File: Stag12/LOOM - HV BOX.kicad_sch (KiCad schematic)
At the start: 15 parts

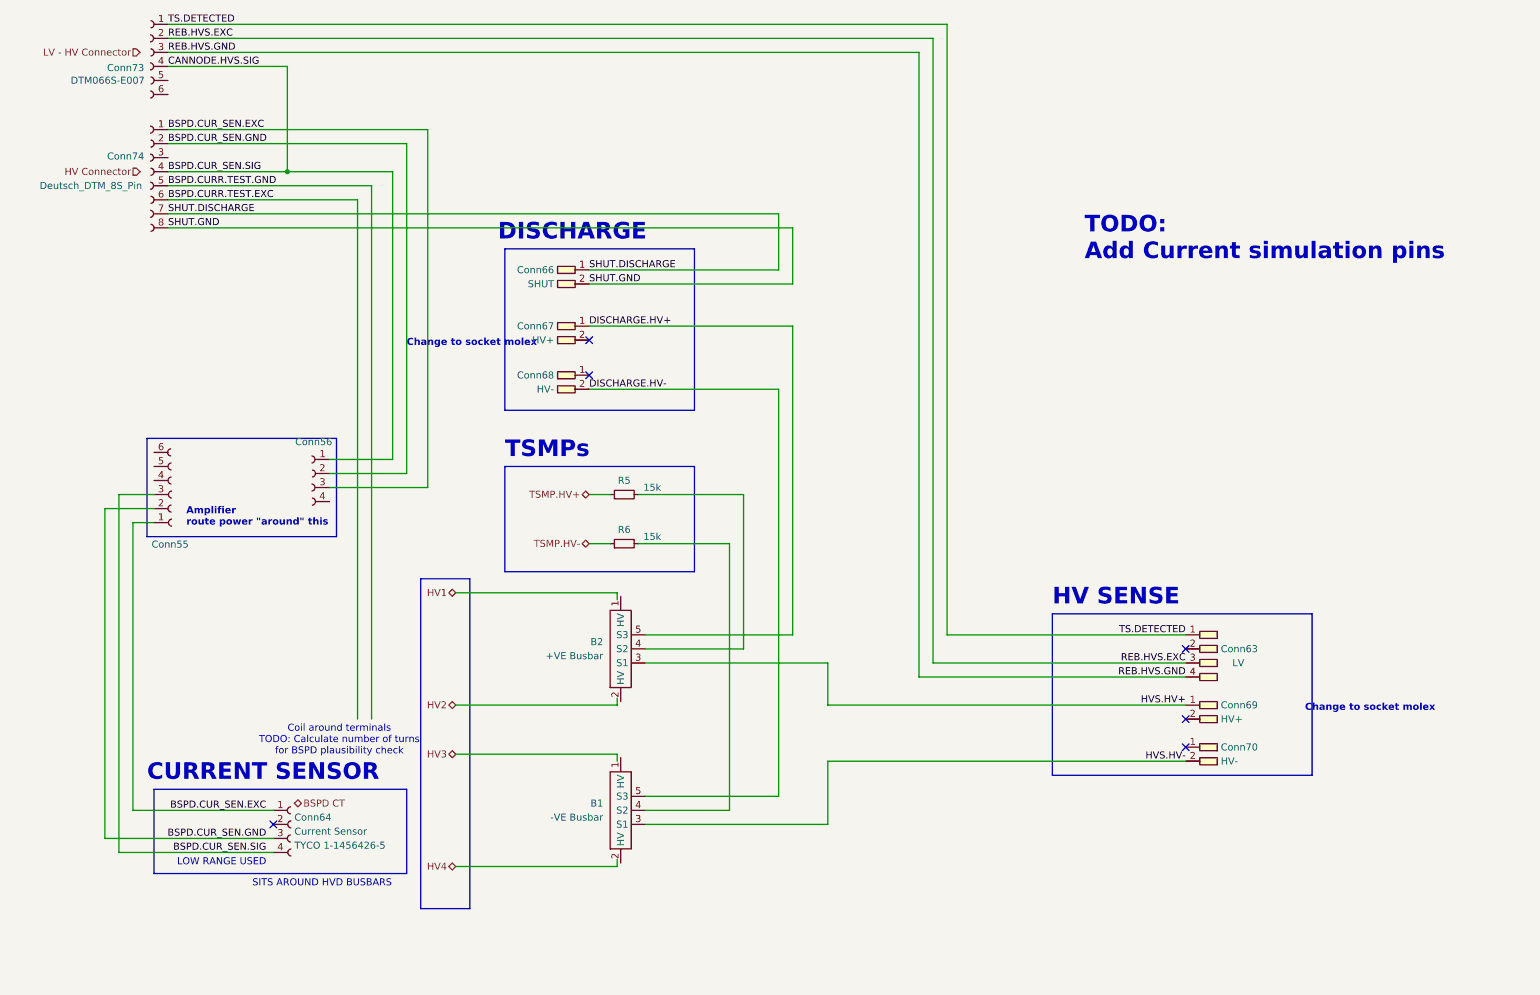
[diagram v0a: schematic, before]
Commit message: HV Box Loom Complete
Moved HVD into HV box, added grounds for cable shield
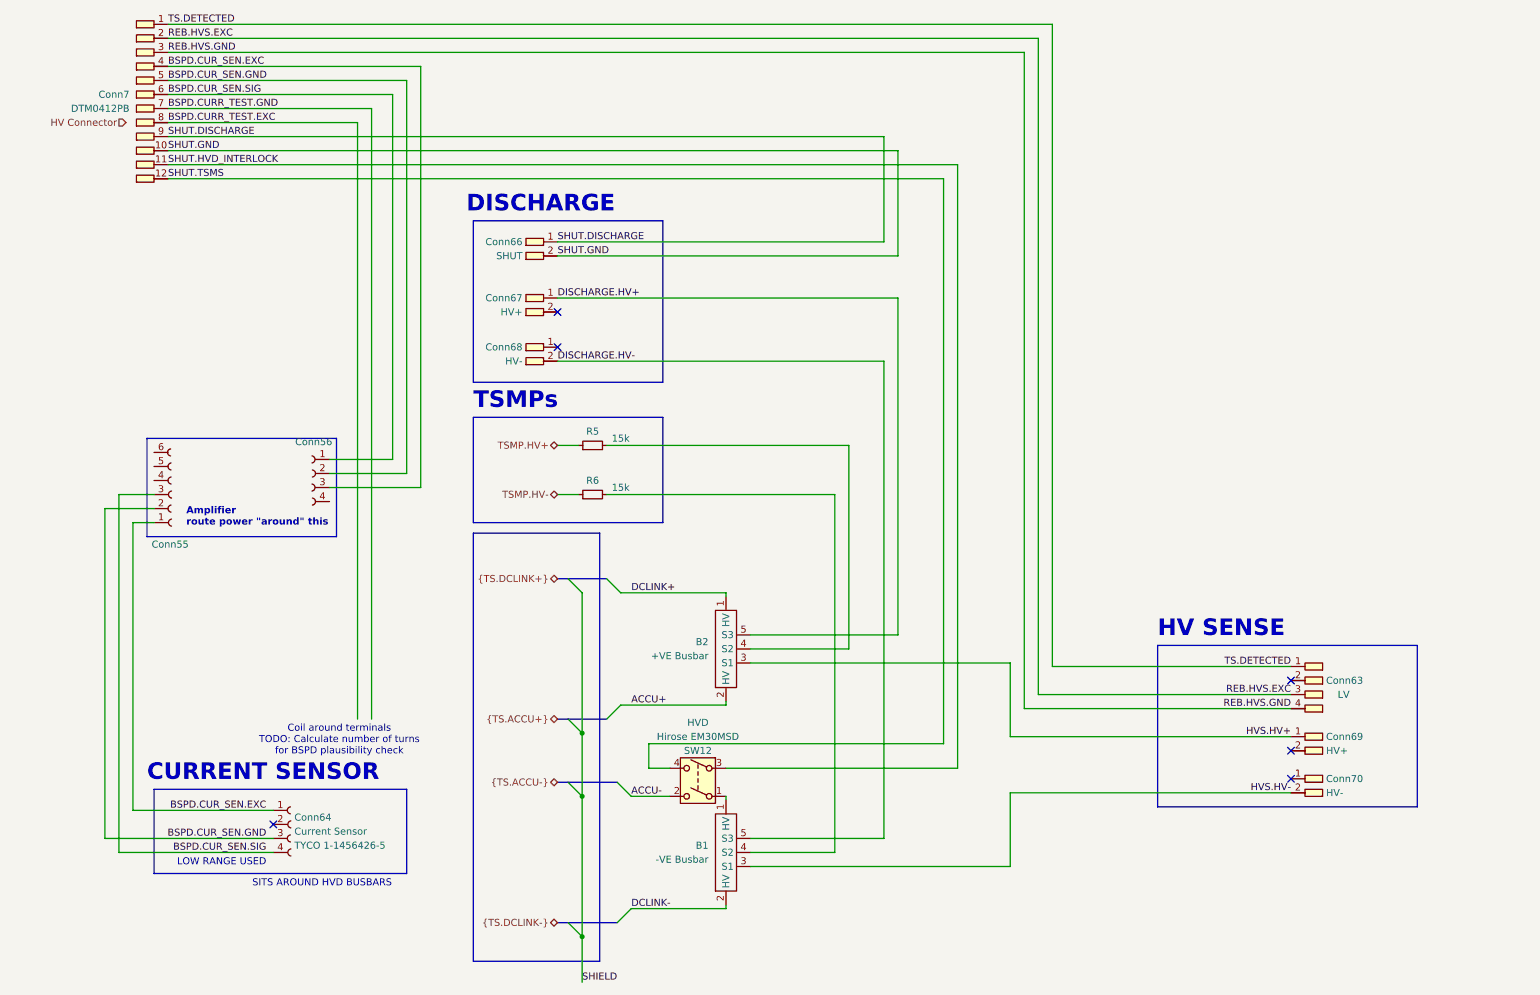
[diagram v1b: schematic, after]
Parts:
- removed Conn73: Deutsch_DTM_12S_Pin, symbol Connectors_SUFST:Deutsch_DTM_6S_Pin
- removed Conn74: Deutsch_DTM_8S_Pin, symbol Connectors_SUFST:Molex_8x1S_Recepticle
- added Conn7: Deutsch_DTM_12P_Pin, symbol Connectors_SUFST:Deutsch_DTM_12P_Pin
- added SW12: Hirose EM30MSD, symbol Switch:SW_DPST
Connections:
- net BSPD.CUR_SEN.EXC: now also Conn7.4
- net BSPD.CUR_SEN.GND: now also Conn7.5
- net BSPD.CUR_SEN.SIG: now also Conn7.6
- net REB.HVS.EXC: now also Conn7.2
- net REB.HVS.GND: now also Conn7.3
- net SHUT.DISCHARGE: now also Conn7.9
- net SHUT.GND: now also Conn7.10
- net TS.DETECTED: now also Conn7.1
- net at B1.1 (HV): now also SW12.1
- net DCLINK-: now reaches B1.2 (HV)
- net DCLINK+: now reaches B2.1 (HV)
- net ACCU+: now reaches B2.2 (HV)
- new net ACCU-: SW12.2
- new net BSPD.CURR_TEST.EXC: Conn7.8
- new net BSPD.CURR_TEST.GND: Conn7.7
- new net SHUT.HVD_INTERLOCK: Conn7.11, SW12.3
- new net SHUT.TSMS: Conn7.12, SW12.4
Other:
- note removed: "Change to socket molex"
- note removed: "TODO: Add Current simulation pins"
- moved on the sheet: B1, B2, Conn63, Conn66, Conn67, Conn68, Conn69, Conn70, R5, R6

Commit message: Added Rear Bulkhead connector
- Updated umbilical to #24
- started moving components to new locations
- some prep work for buses
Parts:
- added L1: L, symbol Device:L
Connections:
- net BSPD.CURR_TEST.EXC renamed BSPD.CURR_TEST+
- net BSPD.CURR_TEST.GND renamed BSPD.CURR_TEST-
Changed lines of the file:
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@@
 		)
 	)
-	(label "BSPD.CURR_TEST.GND"
+	(label "BSPD.CURR_TEST-"
 		(at 39.37 34.29 0)
 		(effects
@@
 		)
 	)
-	(label "BSPD.CURR_TEST.EXC"
+	(label "BSPD.CURR_TEST+"
 		(at 39.37 36.83 0)
 		(effects
@@
 					(unit 1)
 				)
+			)
+		)
+	)
+	(symbol
+		(lib_id "Device:L")
+		(at 74.93 142.875 270)
+		(unit 1)
+		(exclude_from_sim no)
+		(in_bom yes)
+		(on_board yes)
+		(dnp no)
+		(fields_autoplaced yes)
+		(property "Reference" "L1"
+			(at 74.93 138.43 90)
+			(effects
+				(font
+					(size 1.27 1.27)
+				)
+			)
+		)
+		(property "Value" "L"
+			(at 74.93 140.97 90)
+			(effects
+				(font
+					(size 1.27 1.27)
+				)
+			)
+		)
+		(property "Footprint" ""
+			(at 74.93 142.875 0)
+			(effects
+				(font
+					(size 1.27 1.27)
+				)
+				(hide yes)
+			)
+		)
+		(property "Datasheet" "~"
+			(at 74.93 142.875 0)
+			(effects
+				(font
+					(size 1.27 1.27)
+				)
+				(hide yes)
+			)
+		)
+		(property "Description" "Inductor"
+			(at 74.93 142.875 0)
+			(effects
+				(font
+					(size 1.27 1.27)
+				)
+				(hide yes)
+			)
+		)
+		(pin "1"
+		)
+		(pin "2"
+		)
+		(instances
+			(project ""
+				(path "/03011643-0690-4b85-ab78-d6a62dae52b1/8c8ba23c-c17e-4aa5-bc73-bc09925b49ea"
+					(reference "L1")
+					(unit 1)
+				)

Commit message: Started rear loom
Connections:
- net SHUT.HVD_INTERLOCK renamed SHUT.HVD.INTERLOCK
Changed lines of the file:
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@@
 		)
 	)
-	(label "SHUT.HVD_INTERLOCK"
+	(label "SHUT.HVD.INTERLOCK"
 		(at 39.37 44.45 0)
 		(effects

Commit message: More rear loom progress
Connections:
- net REB.HVS.EXC renamed HVSENSE.EXC
- net REB.HVS.GND renamed HVSENSE.GND
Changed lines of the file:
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@@
 		)
 	)
-	(label "REB.HVS.EXC"
+	(label "HVSENSE.EXC"
 		(at 39.37 21.59 0)
 		(effects
@@
 		)
 	)
-	(label "REB.HVS.GND"
+	(label "HVSENSE.GND"
 		(at 39.37 24.13 0)
 		(effects
